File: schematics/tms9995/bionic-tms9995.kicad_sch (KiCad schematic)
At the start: 6 parts, among them J1 Bionic-P135, J2 Bionic-P245, U1 TMS9995, U2 74HCT126, U3 11AA010-I/TO

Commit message: [TMS9995] Update schematics
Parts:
- removed U2: 74HCT126, Package_DIP:DIP-14_W7.62mm, symbol 0-LocalLibrary:74HCT126
- removed U3: 11AA010-I/TO, TO-92_MC_MCH, symbol 0-LocalLibrary:11AA010-I_TO
- added C2: 22U, Capacitor_SMD:C_0603_1608Metric_Pad1.08x0.95mm_HandSolder, symbol Device:C_Small
- added D1: CSL1901UW1, 0-LocalLibrary:LED_CSL1901UW1_ROM-M, symbol 0-LocalLibrary:CSL1901UW1
- added R1: 1.6k, Resistor_SMD:R_0603_1608Metric_Pad0.98x0.95mm_HandSolder, symbol Device:R_Small
- added U2: 11AA010-I/TT, 0-LocalLibrary:SOT-23_MC_MCH-M, symbol 0-LocalLibrary:11AA010-I_TT
- C1: footprint Capacitor_THT:C_Disc_D3.4mm_W2.1mm_P2.50mm -> Capacitor_SMD:C_0603_1608Metric_Pad1.08x0.95mm_HandSolder
- J1: footprint connector:Bionic-P135_Vertical -> 0-LocalLibrary:Bionic-P135_Vertical
- J2: footprint connector:Bionic-P245_Vertical -> 0-LocalLibrary:Bionic-P245_Vertical
- U1: footprint Package_DIP:DIP-40_W15.24mm -> 0-LocalLibrary:DIP-40_W15.24mm_Socket
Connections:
- net GND: now also C2.2, R1.2, U2.3 (VSS)
- net P40: now also U1.20 (~{MEMEN}); no longer U1.18 (~{HOLD})
- net P42: now also U1.19 (~{CRUCLK}/~{WE}); no longer U1.15 (~{INT1})
- net P43: now also U1.16 (IAQ/HOLDA); no longer U1.21 (~{NMI})
- net P46: now also U1.2 (CLKIN)
- net P50: now also U1.21 (~{NMI}); no longer U1.17 (~{DBIN})
- net P51: now also U1.15 (~{INT1}); no longer U1.19 (~{WE})
- net P52: now also U1.14 (~{INT4}/~{EC}); no longer U1.23 (READY)
- net P54: now also U1.23 (READY); no longer U1.20 (~{MEMEN})
- net P55: now also U1.18 (~{HOLD}); no longer U1.16 (IAQ)
- net VCC: now also C2.1, D1.2 (A), U2.2 (VCC)
- net at J2.26 (P57): now also U2.1 (SCIO)
- net P41: now reaches J2.37 (P41)
- net P41: now also U1.17 (~{DBIN})
- net P44: no longer names the net of J2.34 (P44)
- net P44: no longer U1.14 (~{INT4})
- new net: D1.1 (K), R1.1
- no-connect marks 10 -> 7

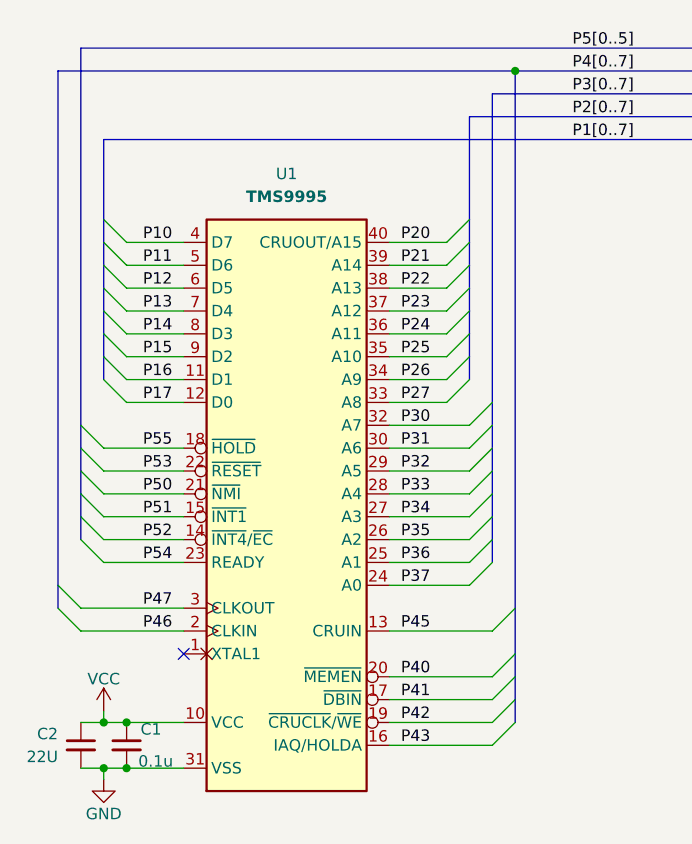
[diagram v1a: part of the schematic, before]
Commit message: [TMS9995] Cleanup schematics
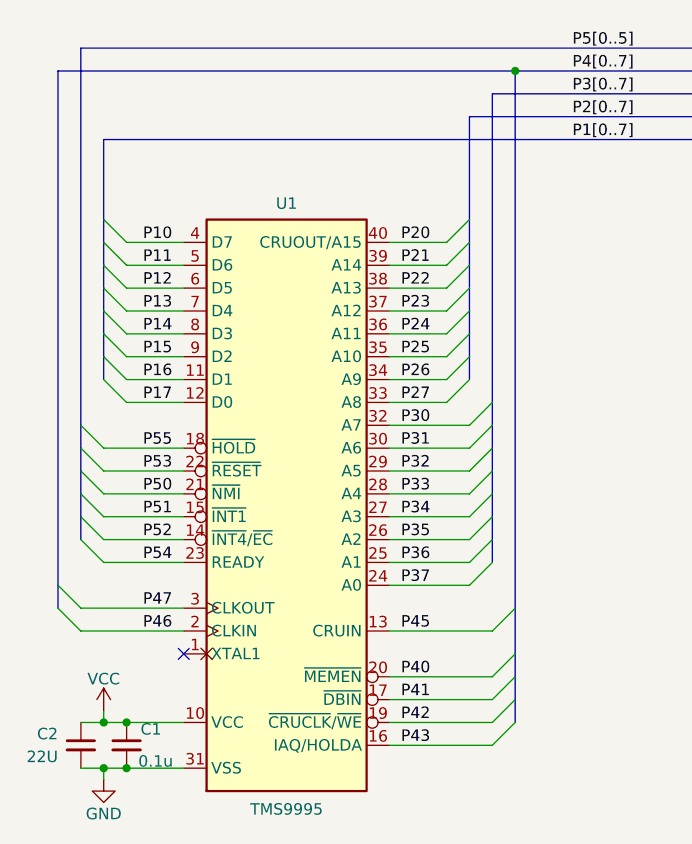
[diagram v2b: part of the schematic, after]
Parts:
- D1: footprint 0-LocalLibrary:LED_CSL1901UW1_ROM-M -> rhom:LED_CSL1901UW1_ROM-M; symbol 0-LocalLibrary:CSL1901UW1 -> rhom:CSL1901UW1
- J1: footprint 0-LocalLibrary:Bionic-P135_Vertical -> bionic:Bionic-P135_Vertical; symbol 0-LocalLibrary:Bionic-P135 -> bionic:Bionic-P135
- J2: footprint 0-LocalLibrary:Bionic-P245_Vertical -> bionic:Bionic-P245_Vertical; symbol 0-LocalLibrary:Bionic-P245 -> bionic:Bionic-P245
- U1: footprint 0-LocalLibrary:DIP-40_W15.24mm_Socket -> bionic:DIP-40_W15.24mm_Socket; symbol 0-LocalLibrary:TMS9995 -> cpu:TMS9995
- U2: footprint 0-LocalLibrary:SOT-23_MC_MCH-M -> microchip:SOT-23_MC_MCH-M; symbol 0-LocalLibrary:11AA010-I_TT -> microchip:11AA010-I_TT
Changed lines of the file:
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@@
 	)
 	(symbol
-		(lib_id "0-LocalLibrary:Bionic-P245")
+		(lib_id "bionic:Bionic-P245")
 		(at 173.99 91.44 0)
 		(unit 1)
@@
 			)
 		)
-		(property "Footprint" "0-LocalLibrary:Bionic-P245_Vertical"
+		(property "Footprint" "bionic:Bionic-P245_Vertical"
 			(at 175.26 127 0)
 			(effects
@@
 	)
 	(symbol
-		(lib_id "0-LocalLibrary:CSL1901UW1")
+		(lib_id "rhom:CSL1901UW1")
 		(at 224.79 38.1 270)
 		(unit 1)
@@
 			)
 		)
-		(property "Footprint" "0-LocalLibrary:LED_CSL1901UW1_ROM-M"
+		(property "Footprint" "rhom:LED_CSL1901UW1_ROM-M"
 			(at 215.9 41.91 0)
 			(effects
@@
 	)
 	(symbol
-		(lib_id "0-LocalLibrary:TMS9995")
+		(lib_id "cpu:TMS9995")
 		(at 100.33 93.98 0)
 		(unit 1)
@@
 		(on_board yes)
 		(dnp no)
-		(fields_autoplaced yes)
 		(property "Reference" "U1"
-			(at 100.33 58.42 0)
+			(at 100.33 61.722 0)
 			(effects
 				(font
@@
 		)
 		(property "Value" "TMS9995"
-			(at 100.33 60.96 0)
-			(effects
-				(font
-					(size 1.27 1.27)
-					(bold yes)
-				)
-			)
-		)
-		(property "Footprint" "0-LocalLibrary:DIP-40_W15.24mm_Socket"
+			(at 100.33 129.032 0)
+			(effects
+				(font
+					(size 1.27 1.27)
+				)
+			)
+		)
+		(property "Footprint" "bionic:DIP-40_W15.24mm_Socket"
 			(at 101.6 128.27 0)
 			(effects
@@
 	)
 	(symbol
-		(lib_id "0-LocalLibrary:Bionic-P135")
+		(lib_id "bionic:Bionic-P135")
 		(at 166.37 91.44 0)
 		(unit 1)
@@
 			)
 		)
-		(property "Footprint" "0-LocalLibrary:Bionic-P135_Vertical"
+		(property "Footprint" "bionic:Bionic-P135_Vertical"
 			(at 167.64 127 0)
 			(effects
@@
 	)
 	(symbol
-		(lib_id "0-LocalLibrary:11AA010-I_TT")
+		(lib_id "microchip:11AA010-I_TT")
 		(at 210.82 64.77 0)
 		(unit 1)
@@
 			)
 		)
-		(property "Footprint" "0-LocalLibrary:SOT-23_MC_MCH-M"
+		(property "Footprint" "microchip:SOT-23_MC_MCH-M"
 			(at 213.36 82.55 0)
 			(effects

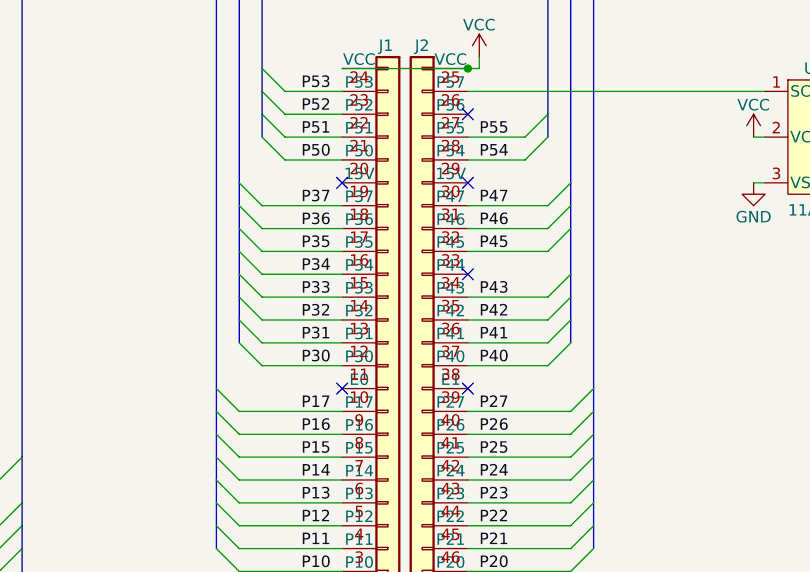
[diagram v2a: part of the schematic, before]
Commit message: [TMS9995] Update schematics
Remove unused pins from bionic connector
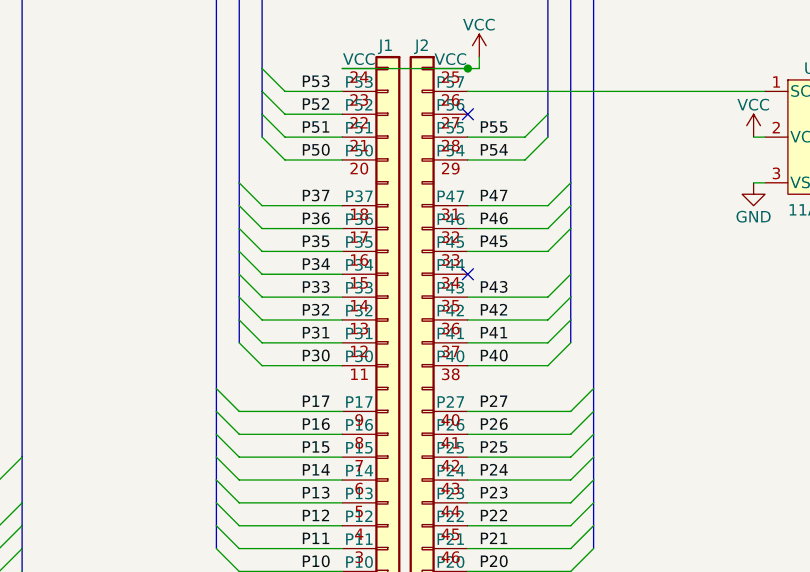
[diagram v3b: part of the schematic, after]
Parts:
- J1: footprint bionic:Bionic-P135_Vertical -> bionic:Bionic-P135_THT
- J2: footprint bionic:Bionic-P245_Vertical -> bionic:Bionic-P245_THT
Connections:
- no-connect marks 7 -> 3
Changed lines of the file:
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@@
 	(title_block
 		(title "BionicTMS9995")
-		(date "2024-12-28")
-		(rev "2")
+		(date "2025-03-02")
+		(rev "3")
 		(company "Tadashi G. Takaoka")
 	)
@@
 	)
 	(no_connect
-		(at 161.29 99.06)
-	)
-	(no_connect
 		(at 175.26 68.58)
 	)
 	(no_connect
-		(at 161.29 76.2)
-	)
-	(no_connect
 		(at 88.9 111.76)
 	)
 	(no_connect
-		(at 175.26 76.2)
-	)
-	(no_connect
-		(at 175.26 99.06)
-	)
-	(no_connect
 		(at 175.26 86.36)
 	)
@@
 			)
 		)
-		(property "Footprint" "bionic:Bionic-P245_Vertical"
+		(property "Footprint" "bionic:Bionic-P245_THT"
 			(at 175.26 127 0)
 			(effects
@@
 		(pin "31"
 		)
-		(pin "30"
-		)
-		(pin "39"
-		)
 		(pin "37"
 		)
@@
 			)
 		)
-		(property "Footprint" "bionic:Bionic-P135_Vertical"
+		(property "Footprint" "bionic:Bionic-P135_THT"
 			(at 167.64 127 0)
 			(effects
@@
 		(pin "13"
 		)
-		(pin "19"
-		)
 		(pin "15"
 		)
-		(pin "10"
-		)
 		(pin "1"
